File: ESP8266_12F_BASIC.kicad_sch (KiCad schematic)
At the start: 37 parts, among them J1 Conn_01x02_Male, J2 Conn_01x04_Male, J3 Conn_01x05_Female, Q1 BC547, U1 ESP-12F, U2 AP1117-33

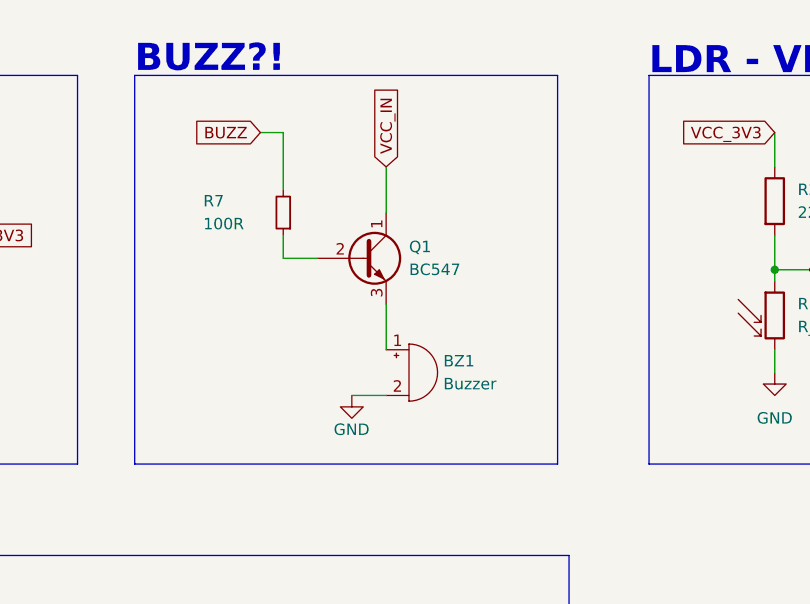
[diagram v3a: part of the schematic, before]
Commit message: fixed stupid npn error
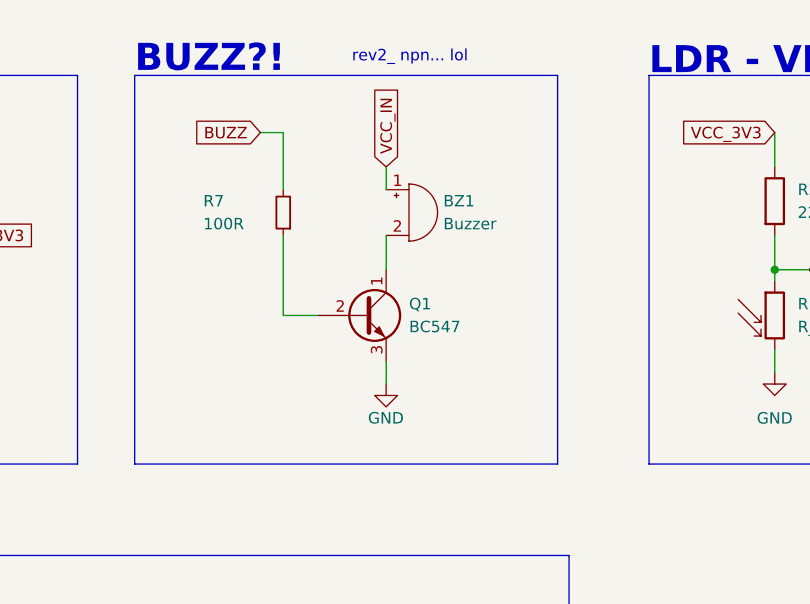
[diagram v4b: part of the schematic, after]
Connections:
- net GND: now also Q1.3 (E); no longer BZ1.2 (+)
- net VCC_IN: now also BZ1.1 (-); no longer Q1.1 (C)
- new net: BZ1.2 (+), Q1.1 (C)
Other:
- note added: "rev2_ npn... lol"
- moved on the sheet: BZ1, Q1
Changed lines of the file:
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@@
+    (stroke (width 0) (type default) (color 0 0 0 0))
+  )
+  (wire (pts (xy 134.62 54.61) (xy 134.62 57.15))
     (stroke (width 0) (type default) (color 0 0 0 0))
   )
@@
     (stroke (width 0) (type default) (color 0 0 0 0))
   )
+  (wire (pts (xy 127 49.53) (xy 123.19 49.53))
+    (stroke (width 0) (type default) (color 0 0 0 0))
+  )
+  (wire (pts (xy 134.62 40.64) (xy 134.62 44.45))
+    (stroke (width 0) (type default) (color 0 0 0 0))
+  )
   (wire (pts (xy 35.56 40.64) (xy 35.56 41.91))
     (stroke (width 0) (type default) (color 0 0 0 0))
@@
     (stroke (width 0) (type default) (color 0 0 0 0))
   )
+  (wire (pts (xy 134.62 33.02) (xy 134.62 35.56))
+    (stroke (width 0) (type default) (color 0 0 0 0))
+  )
   (wire (pts (xy 111.76 115.57) (xy 111.76 114.3))
     (stroke (width 0) (type default) (color 0 0 0 0))
@@
     (stroke (width 0) (type default) (color 0 0 0 0))
   )
-  (wire (pts (xy 134.62 48.26) (xy 134.62 53.34))
-    (stroke (width 0) (type default) (color 0 0 0 0))
-  )
   (wire (pts (xy 36.83 44.45) (xy 33.02 44.45))
     (stroke (width 0) (type default) (color 0 0 0 0))
@@
     (stroke (width 0) (type default) (color 0 0 0 0))
   )
-  (wire (pts (xy 127 43.18) (xy 123.19 43.18))
-    (stroke (width 0) (type default) (color 0 0 0 0))
-  )
   (wire (pts (xy 36.83 48.26) (xy 36.83 44.45))
     (stroke (width 0) (type default) (color 0 0 0 0))
@@
     (stroke (width 0) (type default) (color 0 0 0 0))
   )
-  (wire (pts (xy 130.81 58.42) (xy 134.62 58.42))
-    (stroke (width 0) (type default) (color 0 0 0 0))
-  )
   (wire (pts (xy 105.41 121.92) (xy 105.41 116.84))
     (stroke (width 0) (type default) (color 0 0 0 0))
@@
     (stroke (width 0) (type default) (color 0 0 0 0))
   )
+  (wire (pts (xy 123.19 40.64) (xy 123.19 49.53))
+    (stroke (width 0) (type default) (color 0 0 0 0))
+  )
   (polyline (pts (xy 17.78 149.86) (xy 17.78 193.04))
     (stroke (width 0) (type default) (color 0 0 0 0))
@@
     (stroke (width 0) (type default) (color 0 0 0 0))
   )
-  (wire (pts (xy 134.62 33.02) (xy 134.62 38.1))
-    (stroke (width 0) (type default) (color 0 0 0 0))
-  )
   (wire (pts (xy 83.82 40.64) (xy 83.82 43.18))
     (stroke (width 0) (type default) (color 0 0 0 0))
@@
   )
   (wire (pts (xy 73.66 163.83) (xy 85.09 163.83))
-    (stroke (width 0) (type default) (color 0 0 0 0))
-  )
-  (wire (pts (xy 123.19 43.18) (xy 123.19 40.64))
     (stroke (width 0) (type default) (color 0 0 0 0))
   )
@@
   (text "WS2812B - mehr?" (at 17.78 148.59 0)
     (effects (font (size 3 3) bold) (justify left bottom))
+  )
+  (text "rev2_ npn... lol\n" (at 130.81 21.59 0)
+    (effects (font (size 1.27 1.27)) (justify left bottom))
   )
   (text "U_adc = (3,3V / 320kOhm) * R_ldr\n\n=> U_adc_max = 1,031V\n   U_adc_min ~ 0,01V"
@@
     (pin "1")
   )
-  (symbol (lib_id "power:GND") (at 130.81 58.42 0) (unit 1)
+  (symbol (lib_id "power:GND") (at 134.62 57.15 0) (unit 1)
     (in_bom yes) (on_board yes)
-    (property "Reference" "#PWR09" (id 0) (at 130.81 64.77 0)
-      (effects (font (size 1.27 1.27)) hide)
-    )
-    (property "Value" "GND" (id 1) (at 128.7881 62.2202 0)
-      (effects (font (size 1.27 1.27)) (justify left))
-    )
-    (property "Footprint" "" (id 2) (at 130.81 58.42 0)
-      (effects (font (size 1.27 1.27)) hide)
-    )
-    (property "Datasheet" "" (id 3) (at 130.81 58.42 0)
+    (property "Reference" "#PWR09" (id 0) (at 134.62 63.5 0)
+      (effects (font (size 1.27 1.27)) hide)
+    )
+    (property "Value" "GND" (id 1) (at 132.5981 60.9502 0)
+      (effects (font (size 1.27 1.27)) (justify left))
+    )
+    (property "Footprint" "" (id 2) (at 134.62 57.15 0)
+      (effects (font (size 1.27 1.27)) hide)
+    )
+    (property "Datasheet" "" (id 3) (at 134.62 57.15 0)
       (effects (font (size 1.27 1.27)) hide)
     )
@@
     (pin "2")
   )
-  (symbol (lib_id "Transistor_BJT:BC547") (at 132.08 43.18 0) (unit 1)
-    (in_bom yes) (on_board yes) (fields_autoplaced)
-    (property "Reference" "Q1" (id 0) (at 137.16 41.9099 0)
-      (effects (font (size 1.27 1.27)) (justify left))
-    )
-    (property "Value" "BC547" (id 1) (at 137.16 44.4499 0)
-      (effects (font (size 1.27 1.27)) (justify left))
-    )
-    (property "Footprint" "Package_TO_SOT_THT:TO-92_Inline" (id 2) (at 137.16 45.085 0)
+  (symbol (lib_id "Transistor_BJT:BC547") (at 132.08 49.53 0) (unit 1)
+    (in_bom yes) (on_board yes) (fields_autoplaced)
+    (property "Reference" "Q1" (id 0) (at 137.16 48.2599 0)
+      (effects (font (size 1.27 1.27)) (justify left))
+    )
+    (property "Value" "BC547" (id 1) (at 137.16 50.7999 0)
+      (effects (font (size 1.27 1.27)) (justify left))
+    )
+    (property "Footprint" "Package_TO_SOT_THT:TO-92_Inline" (id 2) (at 137.16 51.435 0)
       (effects (font (size 1.27 1.27) italic) (justify left) hide)
     )
-    (property "Datasheet" "https://www.onsemi.com/pub/Collateral/BC550-D.pdf" (id 3) (at 132.08 43.18 0)
+    (property "Datasheet" "https://www.onsemi.com/pub/Collateral/BC550-D.pdf" (id 3) (at 132.08 49.53 0)
       (effects (font (size 1.27 1.27)) (justify left) hide)
     )
@@
     )
   )
-  (symbol (lib_id "Device:Buzzer") (at 137.16 55.88 0) (unit 1)
-    (in_bom yes) (on_board yes) (fields_autoplaced)
-    (property "Reference" "BZ1" (id 0) (at 140.97 54.6099 0)
-      (effects (font (size 1.27 1.27)) (justify left))
-    )
-    (property "Value" "Buzzer" (id 1) (at 140.97 57.1499 0)
-      (effects (font (size 1.27 1.27)) (justify left))
-    )
-    (property "Footprint" "Buzzer_Beeper:Buzzer_TDK_PS1240P02BT_D12.2mm_H6.5mm" (id 2) (at 136.525 53.34 90)
-      (effects (font (size 1.27 1.27)) hide)
-    )
-    (property "Datasheet" "~" (id 3) (at 136.525 53.34 90)
-      (effects (font (size 1.27 1.27)) hide)
-    )
+  (symbol (lib_id "Device:Buzzer") (at 137.16 38.1 0) (unit 1)
+    (in_bom yes) (on_board yes) (fields_autoplaced)
+    (property "Reference" "BZ1" (id 0) (at 140.97 36.8299 0)
+      (effects (font (size 1.27 1.27)) (justify left))
+    )
+    (property "Value" "Buzzer" (id 1) (at 140.97 39.3699 0)
+      (effects (font (size 1.27 1.27)) (justify left))
+    )
+    (property "Footprint" "Buzzer_Beeper:Buzzer_TDK_PS1240P02BT_D12.2mm_H6.5mm" (id 2) (at 136.525 35.56 90)
+      (effects (font (size 1.27 1.27)) hide)
+    )
+    (property "Datasheet" "~" (id 3) (at 136.525 35.56 90)
+      (effects (font (size 1.27 1.27)) hide)
+    )
